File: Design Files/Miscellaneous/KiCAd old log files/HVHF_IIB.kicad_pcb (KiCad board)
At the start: 4 copper layers, 117 x 79 mm, 64 parts, among them J1 1984963, J2 1984963, J3 731375003, J4 CONSMA002-L, Q1 PNP, Q2 BFP196E6327HTSA1, T1 BFU590G, T10 BFQ252, T11 BFQ252, T12 BFQ252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

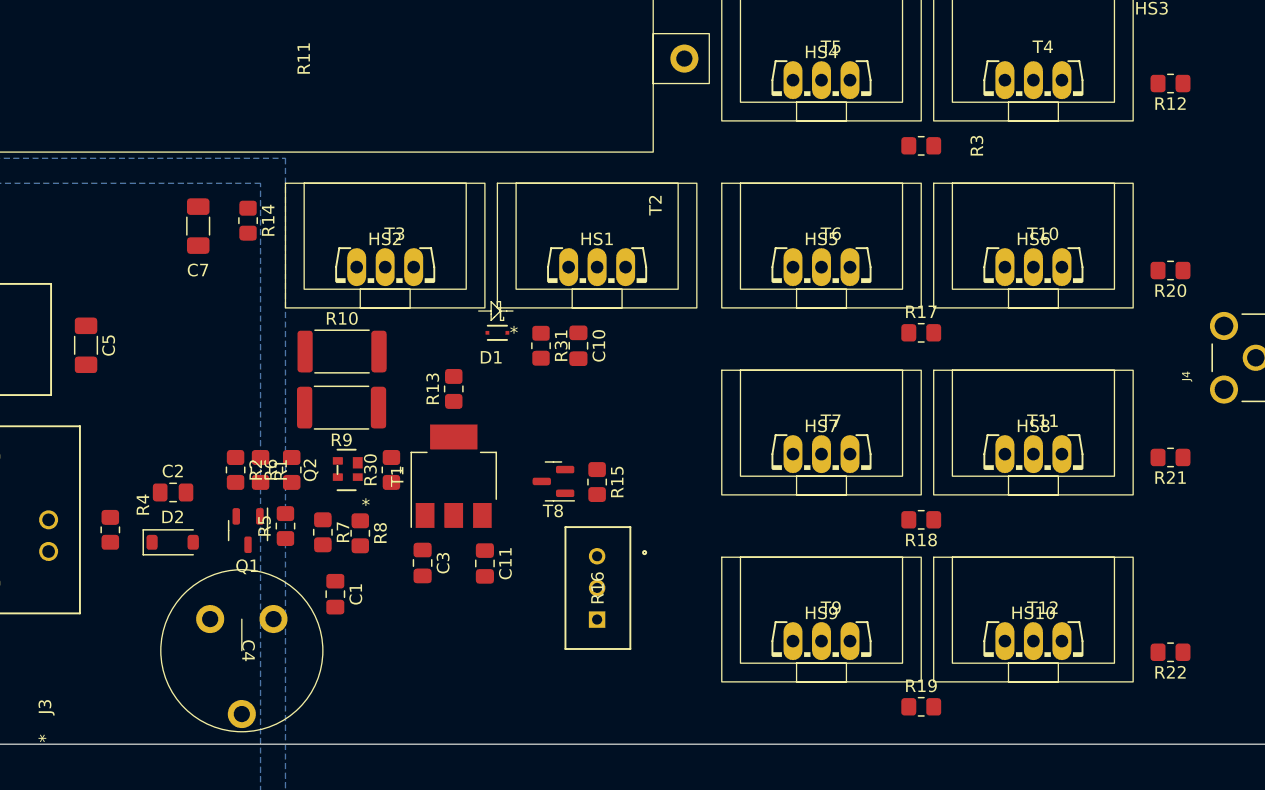
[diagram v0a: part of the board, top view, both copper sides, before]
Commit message: fixed Kicad error
board already open error
moved log files to Miscellaneous folder
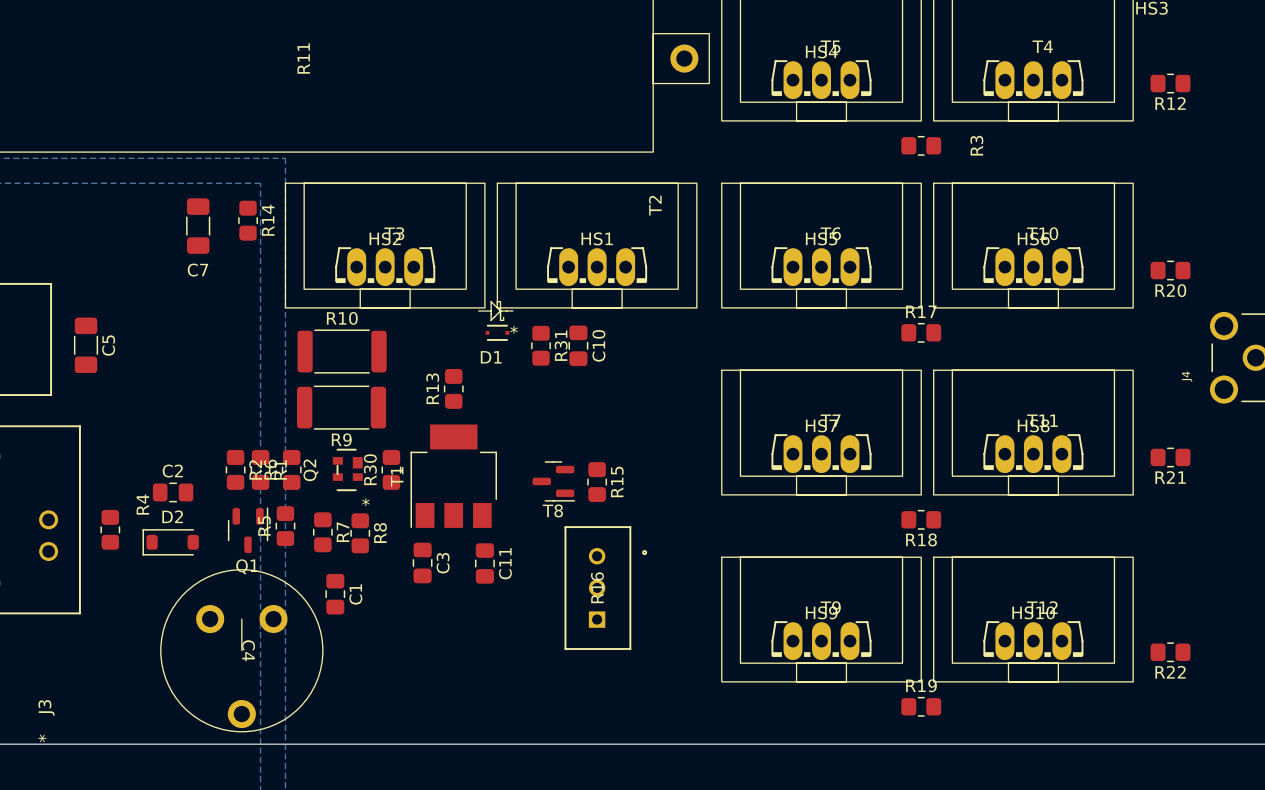
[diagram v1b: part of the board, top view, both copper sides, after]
